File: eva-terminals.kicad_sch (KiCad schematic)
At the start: 24 parts, among them J1 RIBBON, J4 EXTRUDER, J5 HEATER, J6 SPI, J7 AUX, U1 LD39015M33R, U2 ADXL345

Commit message: wip dual ribbon
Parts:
- removed C7: 1U, Capacitor_SMD:C_0805_2012Metric, symbol Device:C
- removed J1: RIBBON, Eagle_WR-MM (rev20b):690367292676, symbol Connector_Generic:Conn_02x13_Odd_Even
- removed J4: EXTRUDER, Eagle_WR-TBL Spring Clamp (rev21a):691402910004B, symbol eva-terminals:Conn_01x04_dual
- removed J7: AUX, Eagle_WR-TBL Spring Clamp (rev21a):691403900004B, symbol eva-terminals:Conn_01x04_dual
- removed JP5: SolderJumper_2_Open, Jumper:SolderJumper-2_P1.3mm_Open_RoundedPad1.0x1.5mm, symbol Jumper:SolderJumper_2_Open
- added C8: 1U, Capacitor_SMD:C_0805_2012Metric, symbol Device:C
- added D1: WS2812B, LED_SMD:LED_WS2812B_PLCC4_5.0x5.0mm_P3.2mm, symbol LED:WS2812B
- added J2: 691403900006B, Eagle_WR-TBL Spring Clamp (rev21a):691403900006B, symbol eva-terminals:Conn_01x06_dualpin
- added J3: Conn_01x04_dualpin, Eagle_WR-TBL Spring Clamp (rev21a):691402910004B, symbol eva-terminals:Conn_01x04_dualpin
- added J6, J7: Conn_02x10_Odd_Even, Eagle_WR-MM (rev20b):690367292076, symbol Connector_Generic:Conn_02x10_Odd_Even
- added JP7, JP8: SolderJumper_2_Open, Jumper:SolderJumper-2_P1.3mm_Open_RoundedPad1.0x1.5mm, symbol Jumper:SolderJumper_2_Open
- added TH1: PT1000, Resistor_SMD:R_1206_3216Metric, symbol Sensor_Temperature:PT1000
- added U3: 74AUP1G32, Package_TO_SOT_SMD:SOT-553, symbol 74xGxx:74AUP1G32
- renumbered LEFT1 to J1, RIGHT1 to J4, J6 to J8
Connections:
- net +3V3: now also U3.5 (VCC); no longer JP6.2 (B)
- net +5V: now also C8.1, D1.1 (VDD), J2.1 (Pin_1), J2.A1 (Pin_1A), J6.6 (Pin_6), J6.8 (Pin_8); no longer J8.2 (Pin_2), J8.A2 (Pin_A2)
- net AUX1: now also J2.4 (Pin_4), J2.A4 (Pin_A4), J6.17 (Pin_17)
- net AUX2: now also J2.5 (Pin_5), J2.A5 (Pin_A5), J6.19 (Pin_19)
- net CS: now also J6.16 (Pin_16), U3.1
- net EXTRUDER_1: now also J3.1 (Pin_1), J3.A1 (Pin_1A), J6.3 (Pin_3)
- net EXTRUDER_2: now also J3.2 (Pin_2), J3.A2 (Pin_A2), J6.1 (Pin_1)
- net EXTRUDER_3: now also J3.3 (Pin_3), J3.A3 (Pin_3), J6.2 (Pin_2)
- net EXTRUDER_4: now also J3.4 (Pin_4), J3.A4 (Pin_A4), J6.4 (Pin_4)
- net GND: now also C8.2, D1.3 (VSS), J2.3 (Pin_3), J2.A3 (Pin_3), J6.5 (Pin_5), J6.7 (Pin_7), J7.10 (Pin_10), J7.3 (Pin_3), J7.4 (Pin_4), U3.3 (GND)
- net HEATER_GND: now also J7.11 (Pin_11), J7.13 (Pin_13), J7.15 (Pin_15), J7.17 (Pin_17), J7.19 (Pin_19)
- net HEATER_PWR: now also J7.12 (Pin_12), J7.14 (Pin_14), J7.16 (Pin_16), J7.18 (Pin_18), J7.20 (Pin_20)
- net PART_FAN_PWM: now also J7.6 (Pin_6)
- net PART_FAN_TACH: now also J7.8 (Pin_8)
- net PROBE: now also J6.14 (Pin_14)
- net PROBE_PWR: now also JP8.1 (A)
- net SCLK: now also J6.15 (Pin_15)
- net SDA: now also U3.2; no longer U2.13 (SDA/SDI/SDIO)
- net SDI: now also J6.18 (Pin_18)
- net SDO: now also J6.13 (Pin_13)
- net TOOL_FAN_GND: now also J7.7 (Pin_7)
- net +12V renamed PART_FAN_PWR
- net PART_FAN_PWR: now also J7.1 (Pin_1), J7.2 (Pin_2); no longer C5.2, J1.1 (Pin_1), J1.A1 (Pin_1A), JP4.2 (B)
- net AUX_PWR renamed NEOPIXEL_IN
- net NEOPIXEL_IN: now also D1.4 (DIN); no longer JP6.1 (A)
- net SENSOR_M renamed GNDREF
- net GNDREF: now also J6.9 (Pin_9), TH1.2
- net SENSOR_P renamed HOTEND_TEMP
- net HOTEND_TEMP: now also J6.11 (Pin_11)
- net TOOL_FAN_TACH renamed TOOL_FAN_TACH/PWM
- net TOOL_FAN_TACH/PWM: now also J7.5 (Pin_5)
- new net: U2.13 (SDA/SDI/SDIO), U3.4
- new net AUX3: J2.6 (Pin_6), J2.A6 (Pin_A6), J6.20 (Pin_20)
- new net CHAMBER_TEMP: J6.12 (Pin_12), J8.2 (Pin_2), J8.A2 (Pin_A2), TH1.1
- new net NEOPIXEL_OUT: D1.2 (DOUT), JP7.2 (B)
- new net NEOPIXEL_RIBBON: J6.10 (Pin_10), JP4.2 (B), JP6.1 (A)
- new net NEOPIXEL_TERMINAL: J2.2 (Pin_2), J2.A2 (Pin_A2), JP6.2 (B), JP7.1 (A)
- new net TOOL_FAN_PWR: C5.2, J1.1 (Pin_1), J1.A1 (Pin_1A), J7.9 (Pin_9), JP8.2 (B)
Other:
- note added: "Dual 20p ribbon cable"
- note added: "Spring terminal blocks"
- moved on the sheet: C4, J1, J4, J5, JP1, JP2, JP3

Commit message: finalized board layout rev 1
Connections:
- net SCL is gone; now on net SCLK: U2.14 (SCL/SCLK)
- net SDA is gone; now on net SDI: U3.2
- net +5V: now also J6.10 (Pin_10), J6.11 (Pin_11); no longer J6.6 (Pin_6), J6.8 (Pin_8)
- net AUX1: now also J6.18 (Pin_18); no longer J6.17 (Pin_17)
- net CHAMBER_TEMP: now also J6.9 (Pin_9), J8.5 (Pin_5), J8.A5 (Pin_A5); no longer J6.12 (Pin_12), J8.2 (Pin_2), J8.A2 (Pin_A2)
- net CS: now also J6.14 (Pin_14), J8.4 (Pin_4), J8.A4 (Pin_A4); no longer J6.16 (Pin_16), J8.6 (Pin_6), J8.A6 (Pin_A6)
- net GND: now also J6.12 (Pin_12), J6.13 (Pin_13), J8.6 (Pin_6), J8.A6 (Pin_A6); no longer J6.5 (Pin_5), J6.7 (Pin_7), J8.1 (Pin_1), J8.A1 (Pin_1A)
- net GNDREF: now also J6.8 (Pin_8); no longer J6.9 (Pin_9)
- net HOTEND_TEMP: now also J6.7 (Pin_7); no longer J6.11 (Pin_11)
- net NEOPIXEL_RIBBON: now also J6.6 (Pin_6); no longer J6.10 (Pin_10)
- net PART_FAN_PWM: now also J7.5 (Pin_5); no longer J7.6 (Pin_6)
- net PART_FAN_TACH: now also J7.6 (Pin_6); no longer J7.8 (Pin_8)
- net PROBE: now also J6.5 (Pin_5); no longer J6.14 (Pin_14)
- net SDI: now also J6.17 (Pin_17), J8.1 (Pin_1), J8.A1 (Pin_1A); no longer J6.18 (Pin_18), J8.4 (Pin_4), J8.A4 (Pin_A4)
- net SDO: now also J6.16 (Pin_16), J8.2 (Pin_2), J8.A2 (Pin_A2); no longer J6.13 (Pin_13), J8.5 (Pin_5), J8.A5 (Pin_A5)
- net TOOL_FAN_PWR: now also J7.8 (Pin_8); no longer J7.9 (Pin_9)
- net TOOL_FAN_TACH/PWM: now also J7.9 (Pin_9); no longer J7.5 (Pin_5)
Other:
- moved on the sheet: J8, JP4

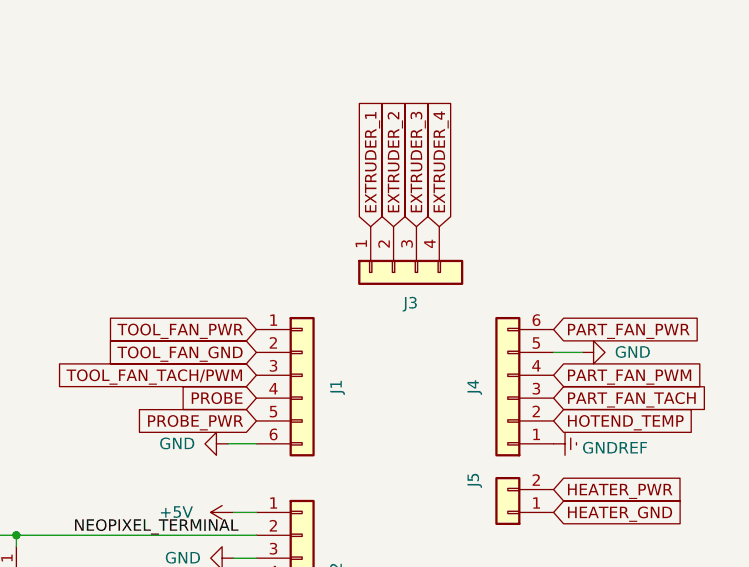
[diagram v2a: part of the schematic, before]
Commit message: jst-xh for stepper
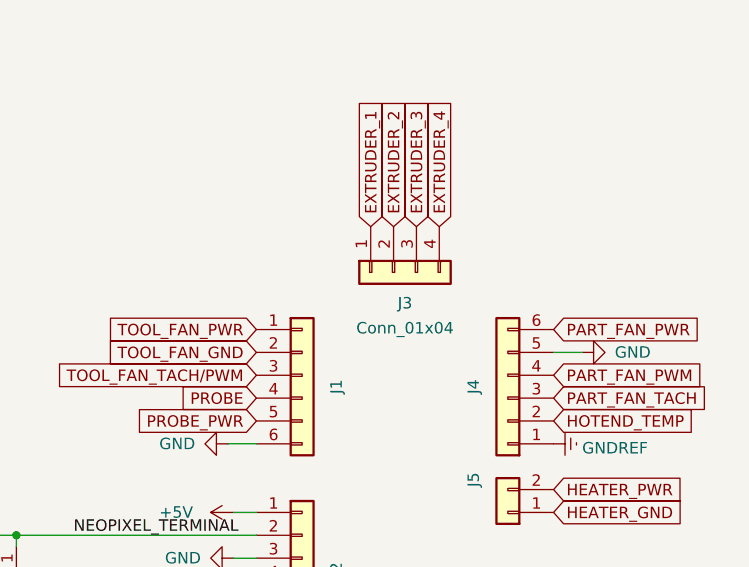
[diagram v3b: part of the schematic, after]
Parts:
- removed J3: Conn_01x04_dualpin, Eagle_WR-TBL Spring Clamp (rev21a):691402910004B, symbol eva-terminals:Conn_01x04_dualpin
- added J3: Conn_01x04, Connector_JST:JST_XH_S4B-XH-A_1x04_P2.50mm_Horizontal, symbol Connector_Generic:Conn_01x04
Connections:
- net EXTRUDER_1: now also J3.1 (Pin_1)
- net EXTRUDER_2: now also J3.2 (Pin_2)
- net EXTRUDER_3: now also J3.3 (Pin_3)
- net EXTRUDER_4: now also J3.4 (Pin_4)
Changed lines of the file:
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@@
     (pin "2")
   )
-  (symbol (lib_id "eva-terminals:Conn_01x04_dualpin") (at 250.19 62.23 90) (mirror x) (unit 1)
-    (in_bom yes) (on_board yes) (fields_autoplaced)
-    (property "Reference" "J3" (id 0) (at 247.015 65.6495 90))
-    (property "Value" "Conn_01x04_dualpin" (id 1) (at 250.19 54.61 0)
-      (effects (font (size 1.27 1.27)) hide)
-    )
-    (property "Footprint" "Eagle_WR-TBL Spring Clamp (rev21a):691402910004B" (id 2) (at 256.54 62.23 0)
-      (effects (font (size 1.27 1.27)) hide)
-    )
-    (property "Datasheet" "~" (id 3) (at 250.19 62.23 0)
+  (symbol (lib_id "power:+5V") (at 111.76 99.06 270) (unit 1)
+    (in_bom yes) (on_board yes) (fields_autoplaced)
+    (property "Reference" "#PWR0110" (id 0) (at 107.95 99.06 0)
+      (effects (font (size 1.27 1.27)) hide)
+    )
+    (property "Value" "+5V" (id 1) (at 114.935 99.539 90)
+      (effects (font (size 1.27 1.27)) (justify left))
+    )
+    (property "Footprint" "" (id 2) (at 111.76 99.06 0)
+      (effects (font (size 1.27 1.27)) hide)
+    )
+    (property "Datasheet" "" (id 3) (at 111.76 99.06 0)
+      (effects (font (size 1.27 1.27)) hide)
+    )
+    (pin "1")
+  )
+  (symbol (lib_id "power:GND") (at 44.45 181.61 0) (unit 1)
+    (in_bom yes) (on_board yes) (fields_autoplaced)
+    (property "Reference" "#PWR0123" (id 0) (at 44.45 187.96 0)
+      (effects (font (size 1.27 1.27)) hide)
+    )
+    (property "Value" "GND" (id 1) (at 44.45 186.1725 0))
+    (property "Footprint" "" (id 2) (at 44.45 181.61 0)
+      (effects (font (size 1.27 1.27)) hide)
+    )
+    (property "Datasheet" "" (id 3) (at 44.45 181.61 0)
+      (effects (font (size 1.27 1.27)) hide)
+    )
+    (pin "1")
+  )
+  (symbol (lib_id "power:GND") (at 226.695 81.28 270) (mirror x) (unit 1)
+    (in_bom yes) (on_board yes)
+    (property "Reference" "#PWR0119" (id 0) (at 220.345 81.28 0)
+      (effects (font (size 1.27 1.27)) hide)
+    )
+    (property "Value" "GND" (id 1) (at 219.075 81.28 90)
+      (effects (font (size 1.27 1.27)) (justify left))
+    )
+    (property "Footprint" "" (id 2) (at 226.695 81.28 0)
+      (effects (font (size 1.27 1.27)) hide)
+    )
+    (property "Datasheet" "" (id 3) (at 226.695 81.28 0)
+      (effects (font (size 1.27 1.27)) hide)
+    )
+    (pin "1")
+  )
+  (symbol (lib_id "power:GND") (at 114.3 167.64 180) (unit 1)
+    (in_bom yes) (on_board yes) (fields_autoplaced)
+    (property "Reference" "#PWR0105" (id 0) (at 114.3 161.29 0)
+      (effects (font (size 1.27 1.27)) hide)
+    )
+    (property "Value" "GND" (id 1) (at 116.205 166.849 0)
+      (effects (font (size 1.27 1.27)) (justify right))
+    )
+    (property "Footprint" "" (id 2) (at 114.3 167.64 0)
+      (effects (font (size 1.27 1.27)) hide)
+    )
+    (property "Datasheet" "" (id 3) (at 114.3 167.64 0)
+      (effects (font (size 1.27 1.27)) hide)
+    )
+    (pin "1")
+  )
+  (symbol (lib_id "power:+5V") (at 227.33 88.9 90) (unit 1)
+    (in_bom yes) (on_board yes)
+    (property "Reference" "#PWR04" (id 0) (at 231.14 88.9 0)
+      (effects (font (size 1.27 1.27)) hide)
+    )
+    (property "Value" "+5V" (id 1) (at 219.075 88.9 90)
+      (effects (font (size 1.27 1.27)) (justify right))
+    )
+    (property "Footprint" "" (id 2) (at 227.33 88.9 0)
+      (effects (font (size 1.27 1.27)) hide)
+    )
+    (property "Datasheet" "" (id 3) (at 227.33 88.9 0)
+      (effects (font (size 1.27 1.27)) hide)
+    )
+    (pin "1")
+  )
+  (symbol (lib_id "Connector_Generic:Conn_01x04") (at 245.11 62.23 90) (mirror x) (unit 1)
+    (in_bom yes) (on_board yes) (fields_autoplaced)
+    (property "Reference" "J3" (id 0) (at 246.38 65.6495 90))
+    (property "Value" "Conn_01x04" (id 1) (at 246.38 68.4246 90))
+    (property "Footprint" "Connector_JST:JST_XH_S4B-XH-A_1x04_P2.50mm_Horizontal" (id 2) (at 245.11 62.23 0)
+      (effects (font (size 1.27 1.27)) hide)
+    )
+    (property "Datasheet" "~" (id 3) (at 245.11 62.23 0)
       (effects (font (size 1.27 1.27)) hide)
     )
@@
     (pin "3")
     (pin "4")
-    (pin "A1")
-    (pin "A2")
-    (pin "A3")
-    (pin "A4")
-  )
-  (symbol (lib_id "power:+5V") (at 111.76 99.06 270) (unit 1)
-    (in_bom yes) (on_board yes) (fields_autoplaced)
-    (property "Reference" "#PWR0110" (id 0) (at 107.95 99.06 0)
-      (effects (font (size 1.27 1.27)) hide)
-    )
-    (property "Value" "+5V" (id 1) (at 114.935 99.539 90)
-      (effects (font (size 1.27 1.27)) (justify left))
-    )
-    (property "Footprint" "" (id 2) (at 111.76 99.06 0)
-      (effects (font (size 1.27 1.27)) hide)
-    )
-    (property "Datasheet" "" (id 3) (at 111.76 99.06 0)
-      (effects (font (size 1.27 1.27)) hide)
-    )
-    (pin "1")
-  )
-  (symbol (lib_id "power:GND") (at 44.45 181.61 0) (unit 1)
-    (in_bom yes) (on_board yes) (fields_autoplaced)
-    (property "Reference" "#PWR0123" (id 0) (at 44.45 187.96 0)
-      (effects (font (size 1.27 1.27)) hide)
-    )
-    (property "Value" "GND" (id 1) (at 44.45 186.1725 0))
-    (property "Footprint" "" (id 2) (at 44.45 181.61 0)
-      (effects (font (size 1.27 1.27)) hide)
-    )
-    (property "Datasheet" "" (id 3) (at 44.45 181.61 0)
-      (effects (font (size 1.27 1.27)) hide)
-    )
-    (pin "1")
-  )
-  (symbol (lib_id "power:GND") (at 226.695 81.28 270) (mirror x) (unit 1)
-    (in_bom yes) (on_board yes)
-    (property "Reference" "#PWR0119" (id 0) (at 220.345 81.28 0)
-      (effects (font (size 1.27 1.27)) hide)
-    )
-    (property "Value" "GND" (id 1) (at 219.075 81.28 90)
-      (effects (font (size 1.27 1.27)) (justify left))
-    )
-    (property "Footprint" "" (id 2) (at 226.695 81.28 0)
-      (effects (font (size 1.27 1.27)) hide)
-    )
-    (property "Datasheet" "" (id 3) (at 226.695 81.28 0)
-      (effects (font (size 1.27 1.27)) hide)
-    )
-    (pin "1")
-  )
-  (symbol (lib_id "power:GND") (at 114.3 167.64 180) (unit 1)
-    (in_bom yes) (on_board yes) (fields_autoplaced)
-    (property "Reference" "#PWR0105" (id 0) (at 114.3 161.29 0)
-      (effects (font (size 1.27 1.27)) hide)
-    )
-    (property "Value" "GND" (id 1) (at 116.205 166.849 0)
-      (effects (font (size 1.27 1.27)) (justify right))
-    )
-    (property "Footprint" "" (id 2) (at 114.3 167.64 0)
-      (effects (font (size 1.27 1.27)) hide)
-    )
-    (property "Datasheet" "" (id 3) (at 114.3 167.64 0)
-      (effects (font (size 1.27 1.27)) hide)
-    )
-    (pin "1")
-  )
-  (symbol (lib_id "power:+5V") (at 227.33 88.9 90) (unit 1)
-    (in_bom yes) (on_board yes)
-    (property "Reference" "#PWR04" (id 0) (at 231.14 88.9 0)
-      (effects (font (size 1.27 1.27)) hide)
-    )
-    (property "Value" "+5V" (id 1) (at 219.075 88.9 90)
-      (effects (font (size 1.27 1.27)) (justify right))
-    )
-    (property "Footprint" "" (id 2) (at 227.33 88.9 0)
-      (effects (font (size 1.27 1.27)) hide)
-    )
-    (property "Datasheet" "" (id 3) (at 227.33 88.9 0)
-      (effects (font (size 1.27 1.27)) hide)
-    )
-    (pin "1")
   )
   (symbol (lib_id "Sensor_Motion:ADXL343") (at 57.15 139.7 0) (unit 1)
@@
       (reference "J2") (unit 1) (value "691403900006B") (footprint "Eagle_WR-TBL Spring Clamp (rev21a):691403900006B")
     )
-    (path "/66f3fa0b-c037-4204-868c-c3a54d0b6ace"
-      (reference "J3") (unit 1) (value "Conn_01x04_dualpin") (footprint "Eagle_WR-TBL Spring Clamp (rev21a):691402910004B")
+    (path "/836c1b72-6495-4f81-a125-58f0f7d787c2"
+      (reference "J3") (unit 1) (value "Conn_01x04") (footprint "Connector_JST:JST_XH_S4B-XH-A_1x04_P2.50mm_Horizontal")
     )
     (path "/a7afa499-79a9-43b3-b557-b38916e6c7cc"

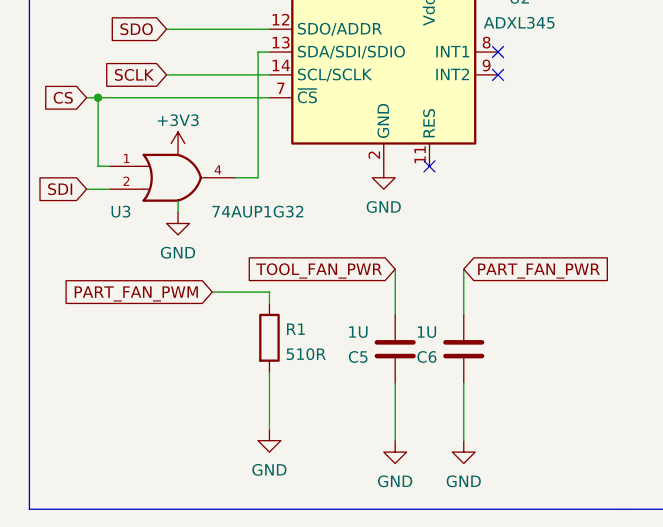
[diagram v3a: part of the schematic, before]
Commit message: change footprint for OR gate
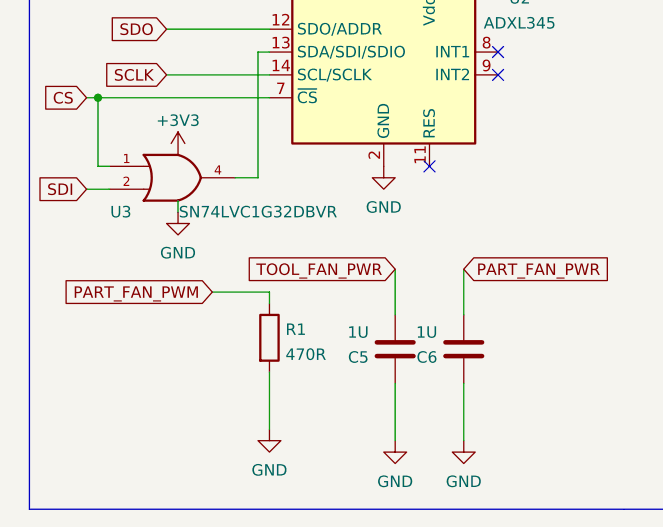
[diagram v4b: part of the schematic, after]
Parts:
- R1: value 510R -> 470R
- U3: value 74AUP1G32 -> SN74LVC1G32DBVR‎; footprint Package_TO_SOT_SMD:SOT-553 -> Package_TO_SOT_SMD:SOT-23-5
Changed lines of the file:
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@@
     (in_bom yes) (on_board yes)
     (property "Reference" "U3" (id 0) (at 27.94 157.48 0))
-    (property "Value" "74AUP1G32" (id 1) (at 43.18 157.48 0))
-    (property "Footprint" "Package_TO_SOT_SMD:SOT-553" (id 2) (at 34.29 153.67 0)
+    (property "Value" "SN74LVC1G32DBVR‎" (id 1) (at 43.18 157.48 0))
+    (property "Footprint" "Package_TO_SOT_SMD:SOT-23-5" (id 2) (at 34.29 153.67 0)
       (effects (font (size 1.27 1.27)) hide)
     )
@@
       (effects (font (size 1.27 1.27)) (justify left))
     )
-    (property "Value" "510R" (id 1) (at 46.228 173.3166 0)
+    (property "Value" "470R" (id 1) (at 46.228 173.3166 0)
       (effects (font (size 1.27 1.27)) (justify left))
     )
@@
     )
     (path "/a3a5d500-c79f-4b63-8e69-81b2d35d3d9a"
-      (reference "R1") (unit 1) (value "510R") (footprint "Resistor_SMD:R_0603_1608Metric")
+      (reference "R1") (unit 1) (value "470R") (footprint "Resistor_SMD:R_0603_1608Metric")
     )
     (path "/8c8d1bce-bec6-4100-a14f-c30abc6be4b9"
@@
     )
     (path "/5fe389a6-3b67-4f61-94e4-0e6947503d87"
-      (reference "U3") (unit 1) (value "74AUP1G32") (footprint "Package_TO_SOT_SMD:SOT-553")
-    )
-  )
+      (reference "U3") (unit 1) (value "SN74LVC1G32DBVR‎") (footprint "Package_TO_SOT_SMD:SOT-23-5")
+    )
+  )
